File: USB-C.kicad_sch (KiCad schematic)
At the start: 25 parts, among them IC5 TPS2557QDRBTQ1, J5 USB_C_Receptacle_USB2.0_16P, J9 USB_A, U2 TPD1E05U06DYA, U3 TPD1E05U06DYA

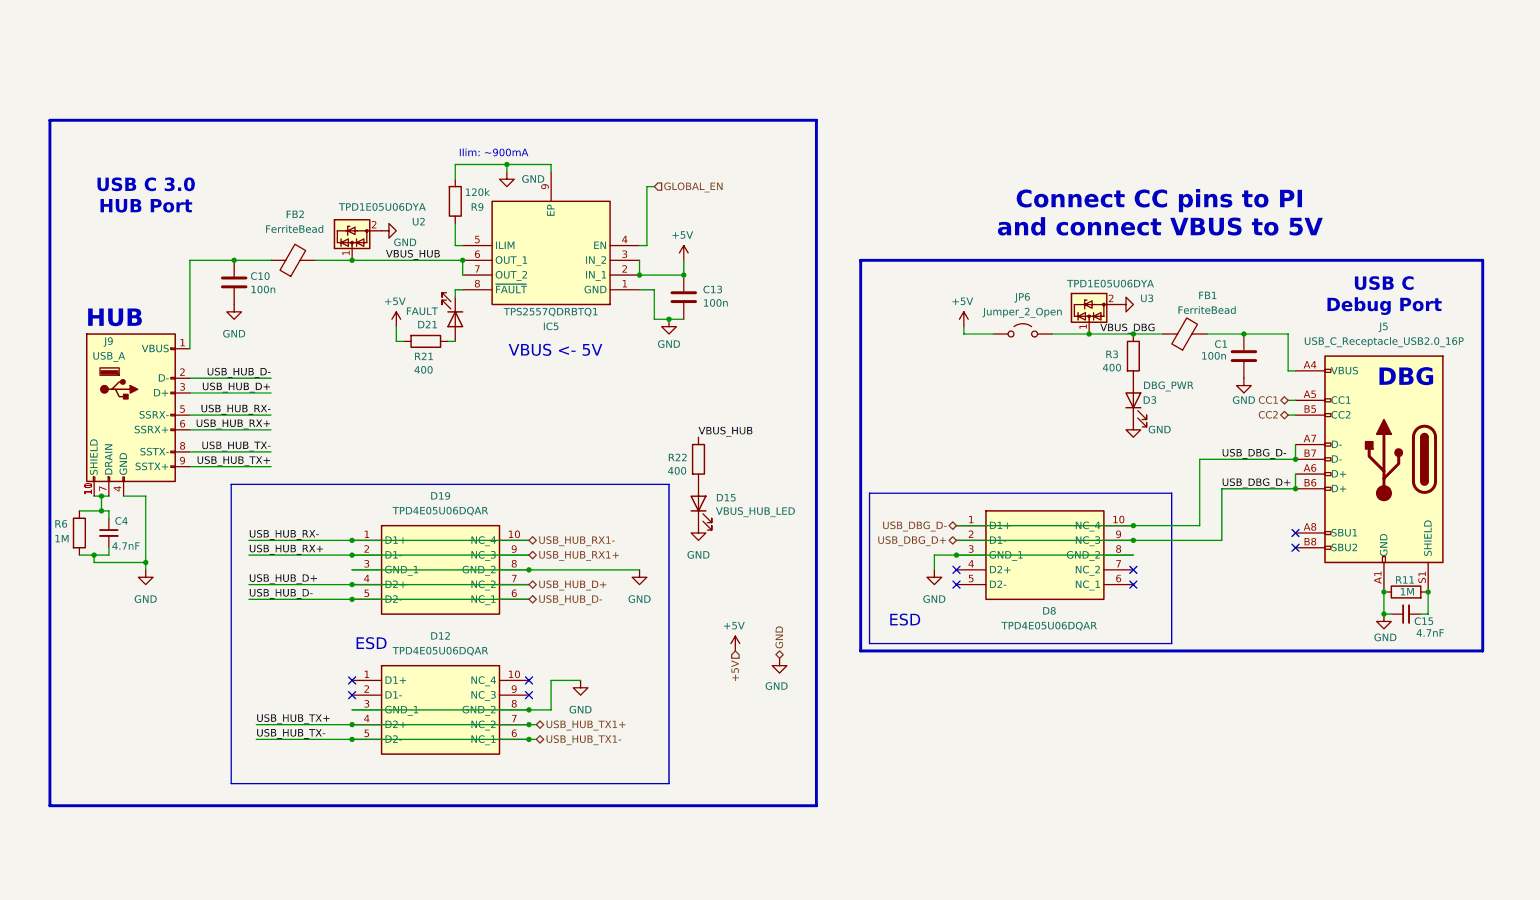
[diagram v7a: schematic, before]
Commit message: ideal diode circuit protection on usbc
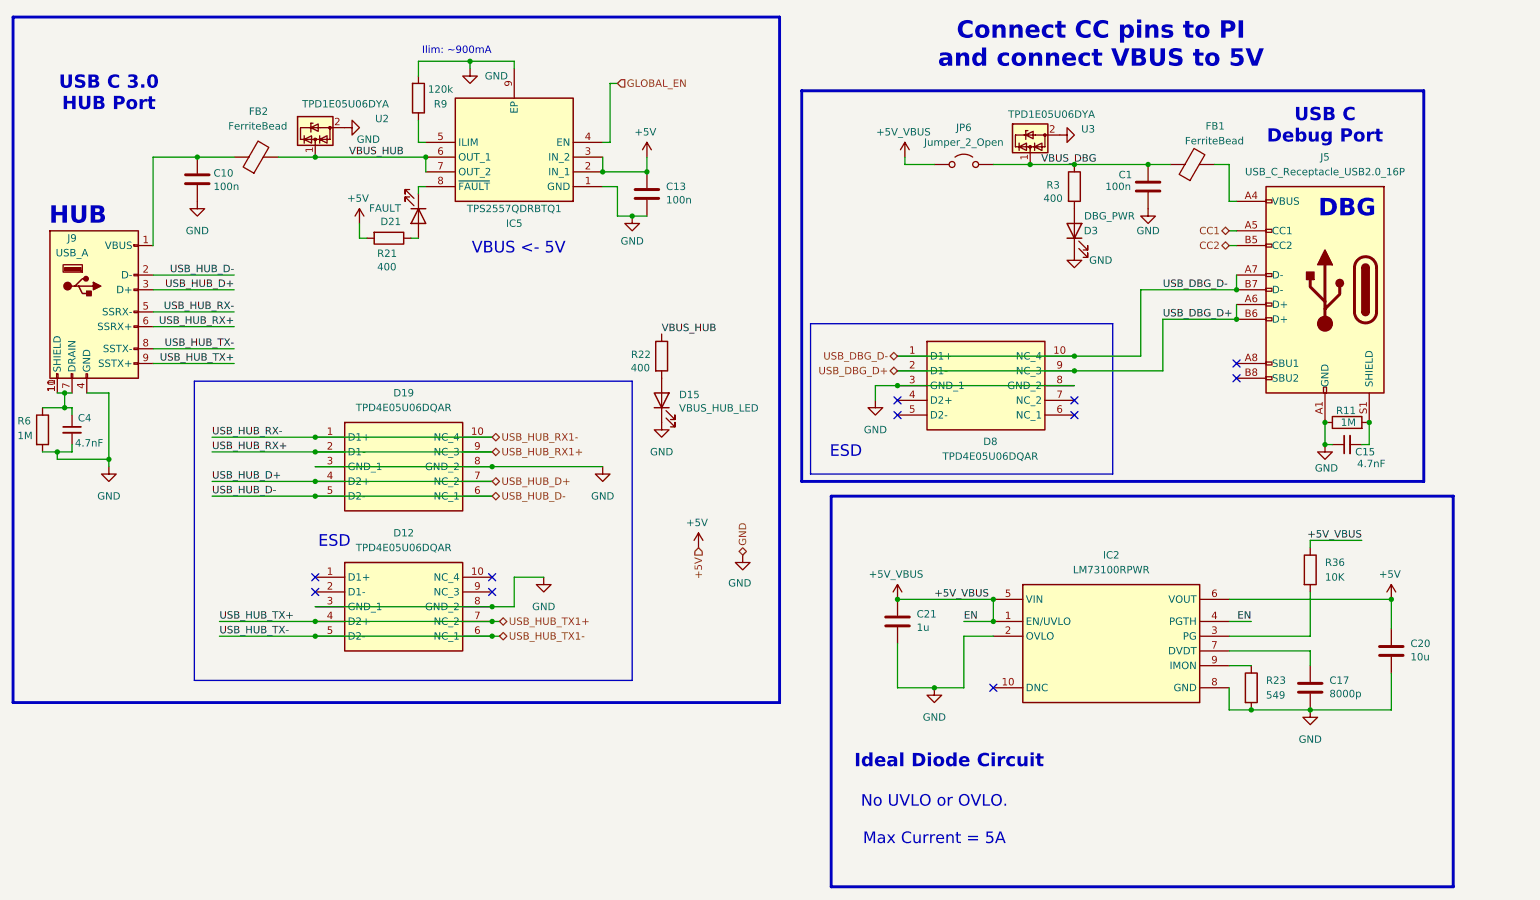
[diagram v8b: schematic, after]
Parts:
- added C17: 8000p, Capacitor_SMD:C_0603_1608Metric_Pad1.08x0.95mm_HandSolder, symbol Device:C
- added C20: 10u, Capacitor_SMD:C_0603_1608Metric_Pad1.08x0.95mm_HandSolder, symbol Device:C
- added C21: 1u, Capacitor_SMD:C_0603_1608Metric_Pad1.08x0.95mm_HandSolder, symbol Device:C
- added IC2: LM73100RPWR, Controls_Pi:LM73100RPWR, symbol LM73100:LM73100RPWR
- added R23: 549, Resistor_SMD:R_0603_1608Metric_Pad0.98x0.95mm_HandSolder, symbol Device:R
- added R36: 10K, Resistor_SMD:R_0603_1608Metric_Pad0.98x0.95mm_HandSolder, symbol Device:R
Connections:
- net +5V: now also C20.1, IC2.6 (VOUT); no longer JP6.1 (A)
- net GND: now also C17.2, C20.2, C21.2, IC2.2 (OVLO), IC2.8 (GND), R23.2
- net VBUS_DBG: now also C1.1
- net at FB1.2, J5.A4 (VBUS), J5.A9 (VBUS)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: no longer C1.1
- new net: C17.1, IC2.7 (DVDT)
- new net: IC2.3 (PG), R36.2
- new net: IC2.9 (IMON), R23.1
- new net +5V_VBUS: C21.1, IC2.1 (EN/UVLO), IC2.4 (PGTH), IC2.5 (VIN), JP6.1 (A), R36.1
- no-connect marks 10 -> 11
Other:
- note added: "Ideal Diode Circuit"
- note added: "No UVLO or OVLO. Max Current = 5A"
- moved on the sheet: C1, C10, C13, C15, C4, D12, D15, D19, D21, D3, D8, FB1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
